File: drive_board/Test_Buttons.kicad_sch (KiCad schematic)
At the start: 45 parts, among them Q1 AO3401A, Q2 AO3401A, Q3 AO3401A, Q4 AO3401A, Q5 AO3401A, Q6 AO3401A, Q7 AO3401A, Q8 AO3401A, SW1 SW_Push, SW2 SW_Push, SW3 SW_Push, SW4 SW_Push

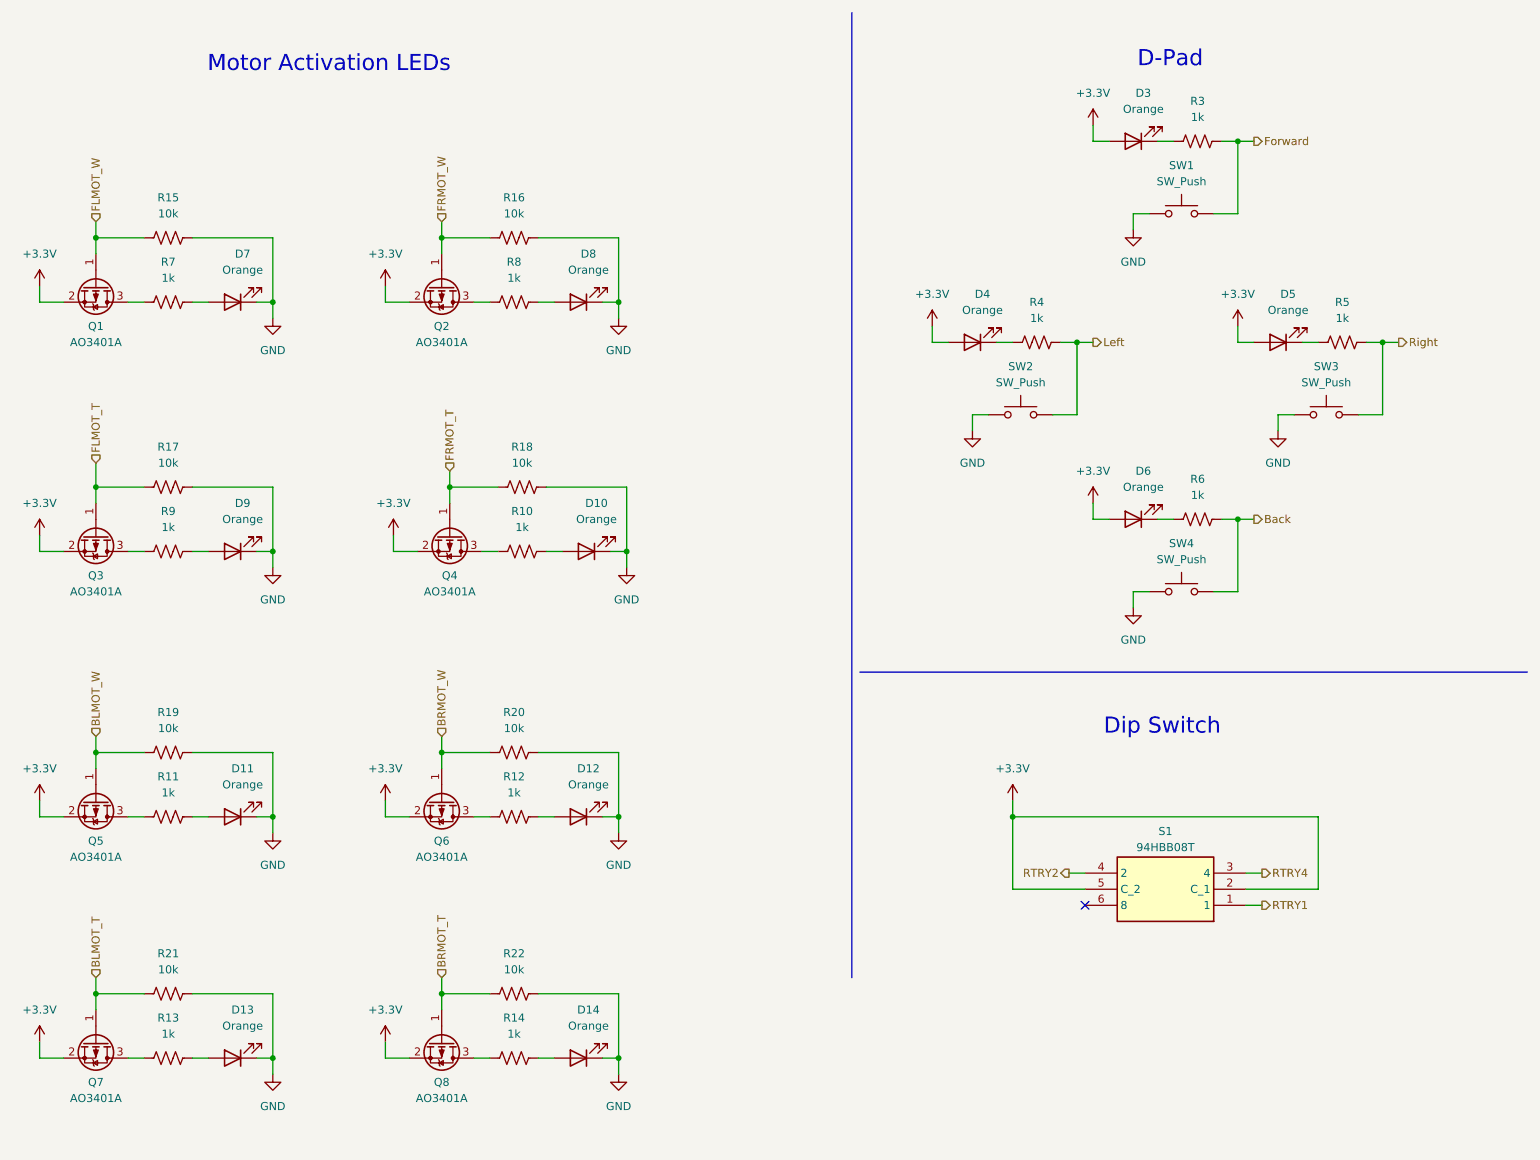
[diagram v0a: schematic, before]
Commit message: Change Testing Control Scheme
- Removed testing D-pad.
- Removed rotary encoder.
- Added two complete (maybe) joystick potentiometer circuits.
- Added dip switch (no circuit).
- Assigned some footprints.
- Grounded mounting holes.
- Added CAN transceiver terminating resistor (footprint only).
- Other stuff I prob forgot.
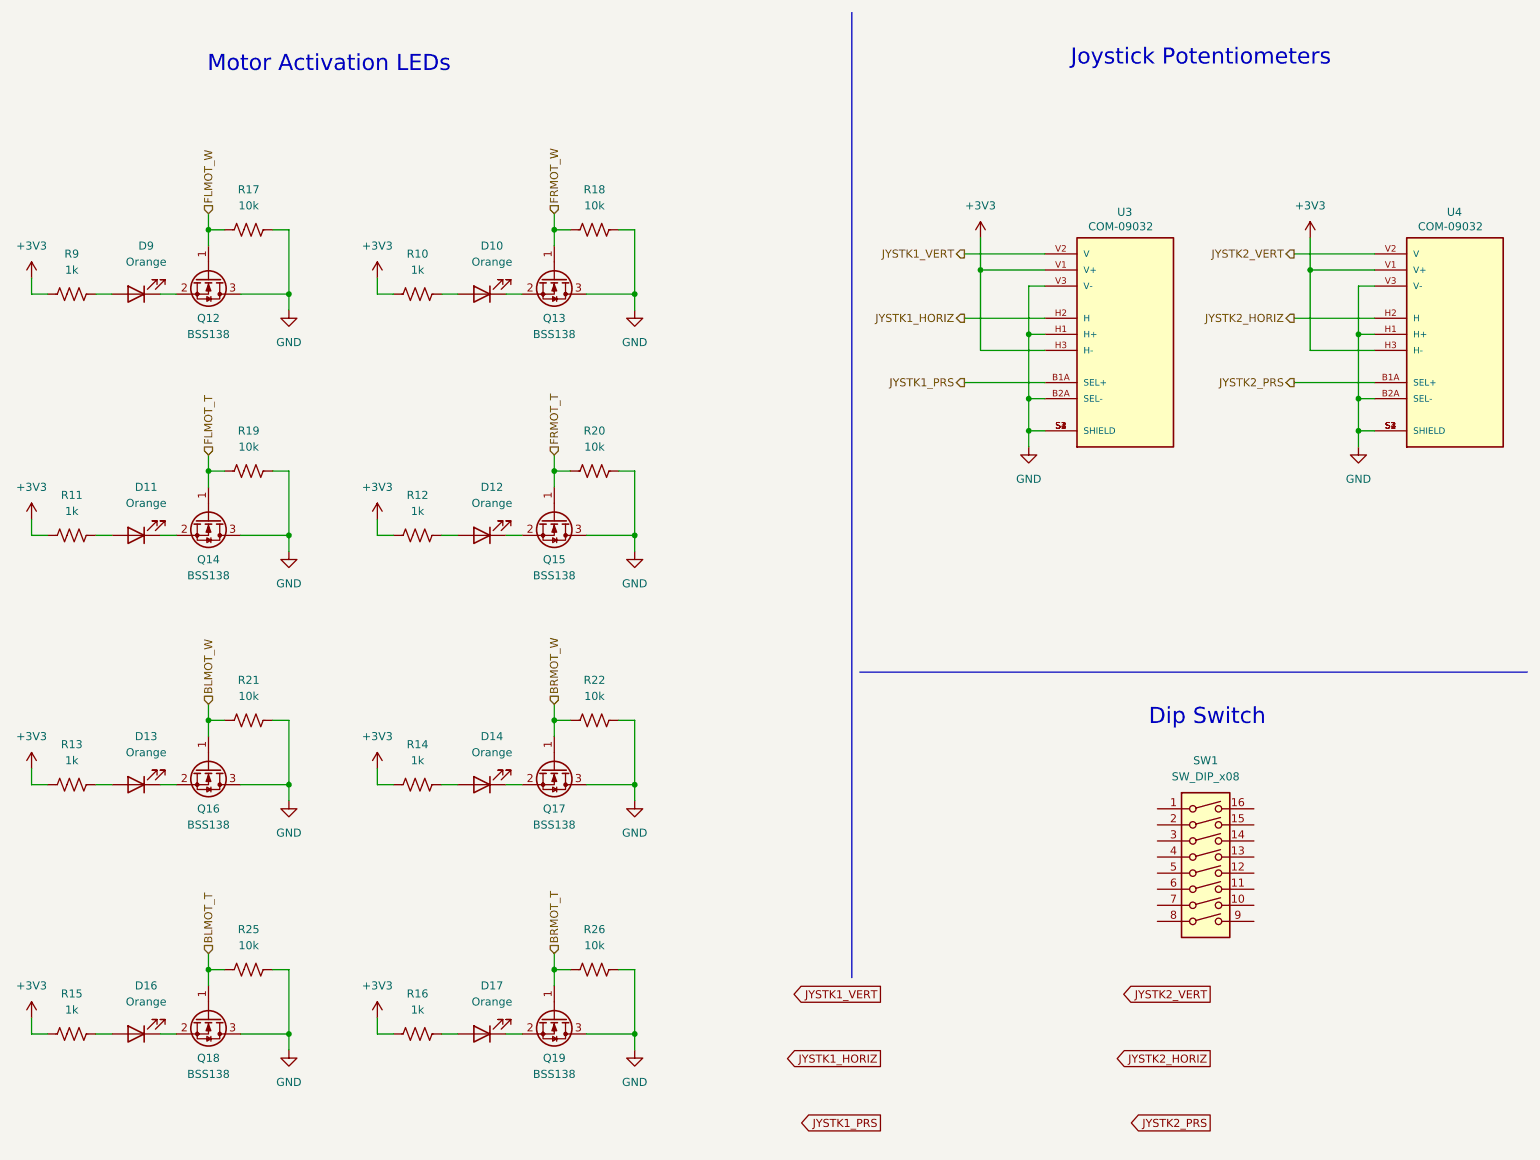
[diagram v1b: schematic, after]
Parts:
- removed D3, D4, D5, D6, D7, D8: Orange, symbol Device:LED
- removed Q1, Q2, Q3, Q4, Q5, Q6, Q7, Q8: AO3401A, Package_TO_SOT_SMD:SOT-23, symbol Transistor_FET:AO3401A
- removed R3, R4, R5, R6: 1k, Resistor_SMD:R_0603_1608Metric_Pad0.98x0.95mm_HandSolder, symbol Device:R_US
- removed R7, R8: 1k, symbol Device:R_US
- removed S1: 94HBB08T, CoreBoard:DIPS762W56P254L991H597Q6N, symbol CoreBoard:94HBB08T
- removed SW1, SW2, SW3, SW4: SW_Push, Button_Switch_SMD:SW_SPST_TL3305A, symbol Switch:SW_Push
- added D16, D17: Orange, LED_SMD:LED_0603_1608Metric_Pad1.05x0.95mm_HandSolder, symbol Device:LED
- added Q12, Q13, Q14, Q15, Q16, Q17, Q18, Q19: BSS138, Package_TO_SOT_SMD:SOT-23, symbol Transistor_FET:BSS138
- added R25, R26: 10k, Resistor_SMD:R_0603_1608Metric_Pad0.98x0.95mm_HandSolder, symbol Device:R_US
- added SW1: SW_DIP_x08, symbol Switch:SW_DIP_x08
- added U3, U4: COM-09032, ps4:XDCR_COM-09032, symbol COM-09032:COM-09032
- D10, D11, D12, D13, D14, D9: footprint (none) -> LED_SMD:LED_0603_1608Metric_Pad1.05x0.95mm_HandSolder
- R10, R11, R12, R13, R14, R17, R18, R19, R20, R21, R22, R9: footprint (none) -> Resistor_SMD:R_0603_1608Metric_Pad0.98x0.95mm_HandSolder
- R15, R16: value 10k -> 1k; footprint (none) -> Resistor_SMD:R_0603_1608Metric_Pad0.98x0.95mm_HandSolder
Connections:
- net BLMOT_T: now also Q18.1 (G), R25.1; no longer R21.1
- net BLMOT_W: now also R21.1, Q16.1 (G); no longer R19.1
- net BRMOT_T: now also Q19.1 (G), R26.1; no longer R22.1
- net BRMOT_W: now also R22.1, Q17.1 (G); no longer R20.1
- net FLMOT_T: now also R19.1, Q14.1 (G); no longer R17.1
- net FLMOT_W: now also R17.1, Q12.1 (G); no longer R15.1
- net FRMOT_T: now also R20.1, Q15.1 (G); no longer R18.1
- net FRMOT_W: now also R18.1, Q13.1 (G); no longer R16.1
- net GND: now also Q12.3 (D), Q13.3 (D), Q14.3 (D), Q15.3 (D), Q16.3 (D), Q17.3 (D), Q18.3 (D), Q19.3 (D), R25.2, R26.2, U3.B2A (SEL-), U3.H1 (H+), U3.S1 (SHIELD), U3.S2 (SHIELD), U3.S3 (SHIELD), U3.S4 (SHIELD), U3.V3 (V-), U4.B2A (SEL-), U4.H1 (H+), U4.S1 (SHIELD), U4.S2 (SHIELD), U4.S3 (SHIELD), U4.S4 (SHIELD), U4.V3 (V-); no longer D10.1 (K), D11.1 (K), D12.1 (K), D13.1 (K), D14.1 (K), D9.1 (K), R15.2, R16.2
- net +3V3: now reaches R13.1
- net +3V3: now also R10.1, R11.1, R12.1, R14.1, R15.1, R16.1, R9.1, U3.H3 (H-), U3.V1 (V+), U4.H3 (H-), U4.V1 (V+)
- new net: D9.1 (K), Q12.2 (S)
- new net: D12.1 (K), Q15.2 (S)
- new net: D10.1 (K), Q13.2 (S)
- new net: D16.1 (K), Q18.2 (S)
- new net: D16.2 (A), R15.2
- new net: D13.1 (K), Q16.2 (S)
- new net: D14.1 (K), Q17.2 (S)
- new net: D17.2 (A), R16.2
- new net: D17.1 (K), Q19.2 (S)
- new net: D11.1 (K), Q14.2 (S)
- new net JYSTK1_HORIZ: U3.H2 (H)
- new net JYSTK1_PRS: U3.B1A (SEL+)
- new net JYSTK1_VERT: U3.V2 (V)
- new net JYSTK2_HORIZ: U4.H2 (H)
- new net JYSTK2_PRS: U4.B1A (SEL+)
- new net JYSTK2_VERT: U4.V2 (V)
- no-connect marks 1 -> 0
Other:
- note added: "Joystick Potentiometers"
- note removed: "D-Pad"

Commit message: Finish Schematic
- Assigned all footprints
- Added dipswitch and connected to RoveNode
- Updated PCB from schematic
- Added absolute encoder pins and connected to RoveNode
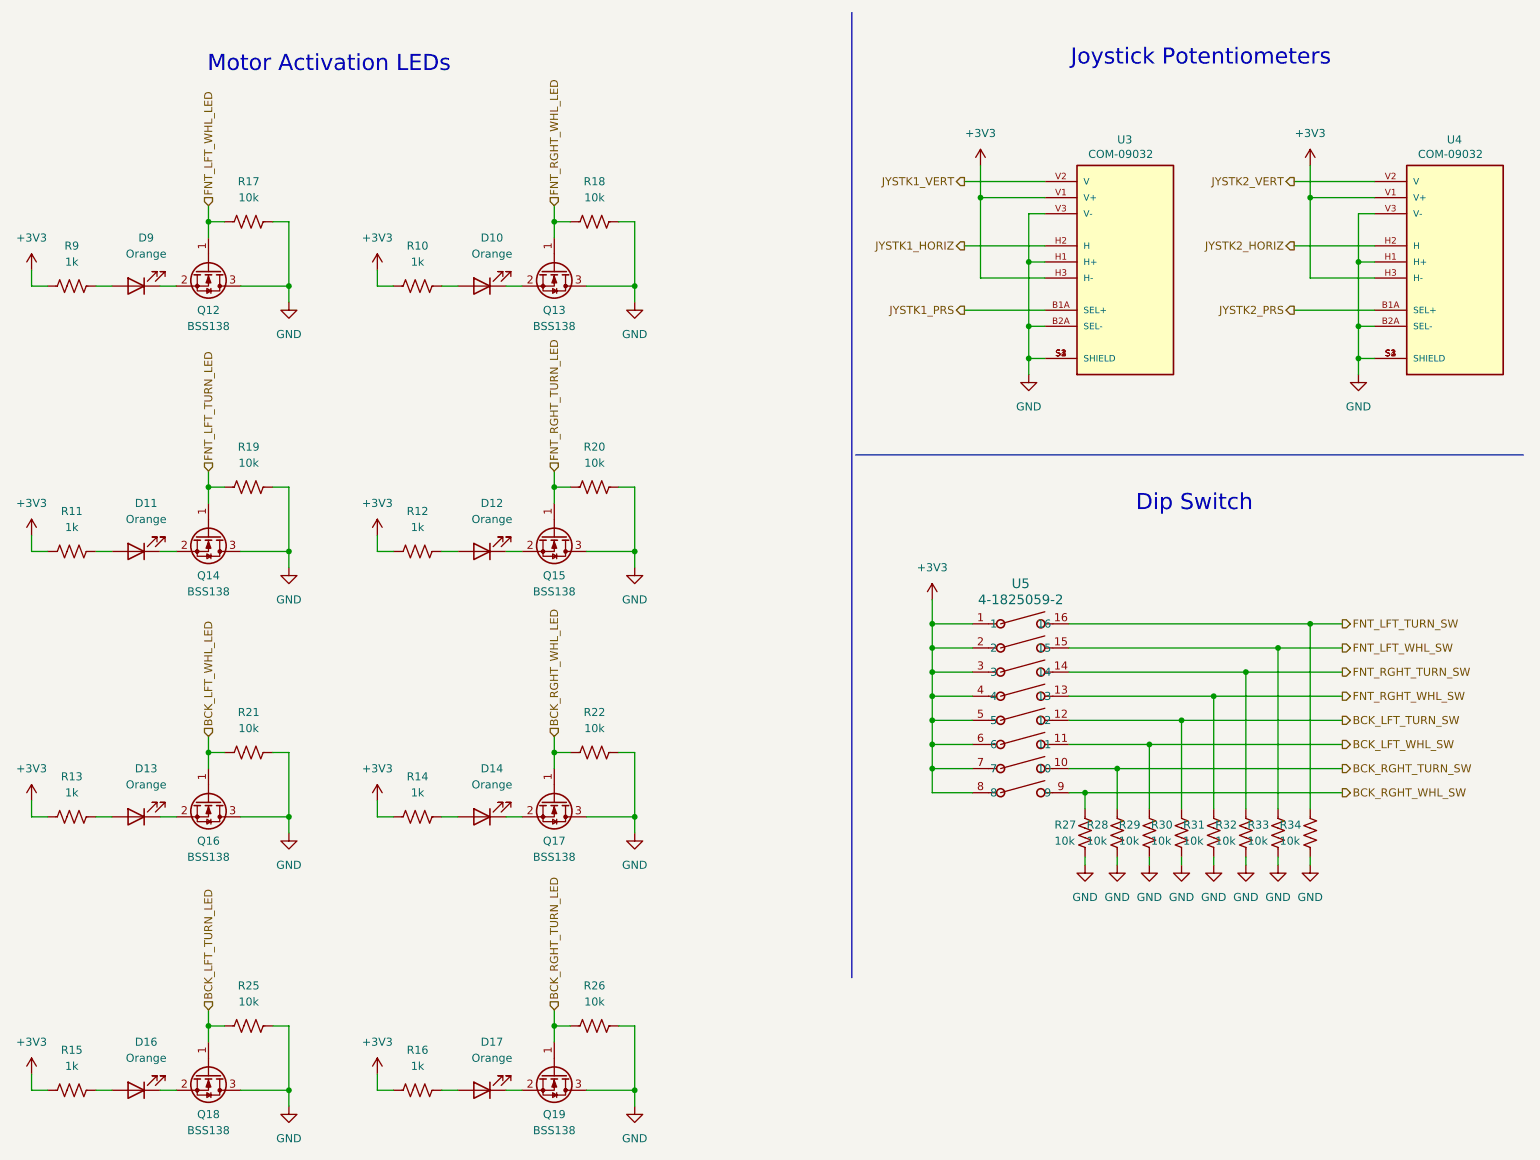
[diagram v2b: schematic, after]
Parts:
- removed SW1: SW_DIP_x08, symbol Switch:SW_DIP_x08
- added R27, R28, R29, R30, R31, R32, R33, R34: 10k, Resistor_SMD:R_0603_1608Metric_Pad0.98x0.95mm_HandSolder, symbol Device:R_US
- added U5: 4-1825059-2, Dipswitch:SWSO16_325X138P100, symbol dipswitch1x8:4-1825059-2
- U3, U4: footprint ps4:XDCR_COM-09032 -> Joystick:XDCR_COM-09032
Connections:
- net +3V3: now also U5.1, U5.2, U5.3, U5.4, U5.5, U5.6, U5.7, U5.8
- net GND: now also R27.1, R28.1, R29.1, R30.1, R31.1, R32.1, R33.1, R34.1
- net BLMOT_T renamed BCK_LFT_TURN_LED
- net BLMOT_W renamed BCK_LFT_WHL_LED
- net BRMOT_T renamed BCK_RGHT_TURN_LED
- net BRMOT_W renamed BCK_RGHT_WHL_LED
- net FLMOT_T renamed FNT_LFT_TURN_LED
- net FLMOT_W renamed FNT_LFT_WHL_LED
- net FRMOT_T renamed FNT_RGHT_TURN_LED
- net FRMOT_W renamed FNT_RGHT_WHL_LED
- new net BCK_LFT_TURN_SW: R30.2, U5.12
- new net BCK_LFT_WHL_SW: R29.2, U5.11
- new net BCK_RGHT_TURN_SW: R28.2, U5.10
- new net BCK_RGHT_WHL_SW: R27.2, U5.9
- new net FNT_LFT_TURN_SW: R34.2, U5.16
- new net FNT_LFT_WHL_SW: R33.2, U5.15
- new net FNT_RGHT_TURN_SW: R32.2, U5.14
- new net FNT_RGHT_WHL_SW: R31.2, U5.13
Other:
- moved on the sheet: D10, D11, D12, D13, D14, D16, D17, D9, Q12, Q13, Q14, Q15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
